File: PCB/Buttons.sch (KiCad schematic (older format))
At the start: 15 parts

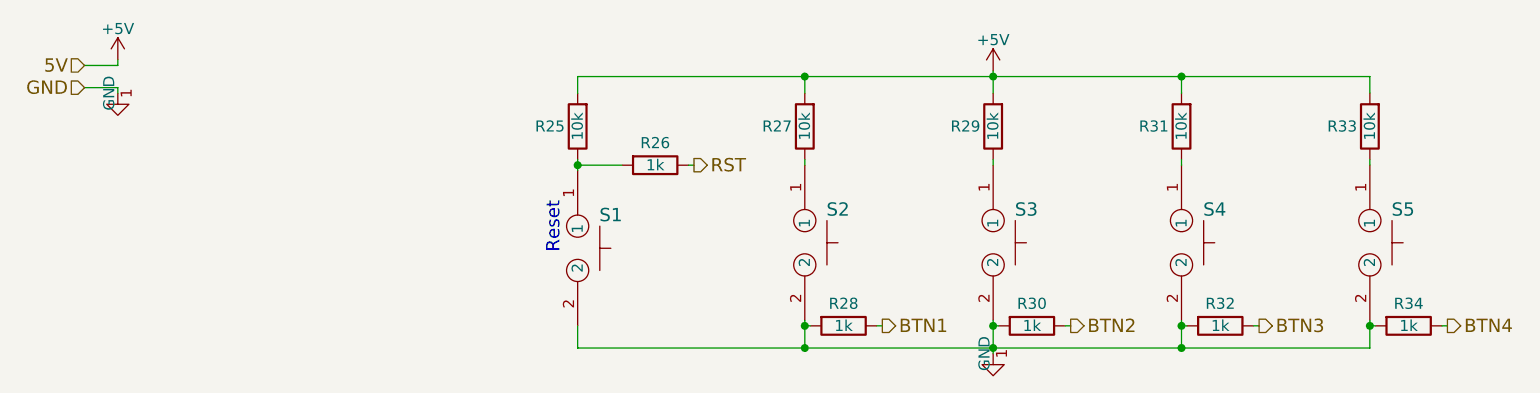
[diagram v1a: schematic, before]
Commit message: Added PCB layout
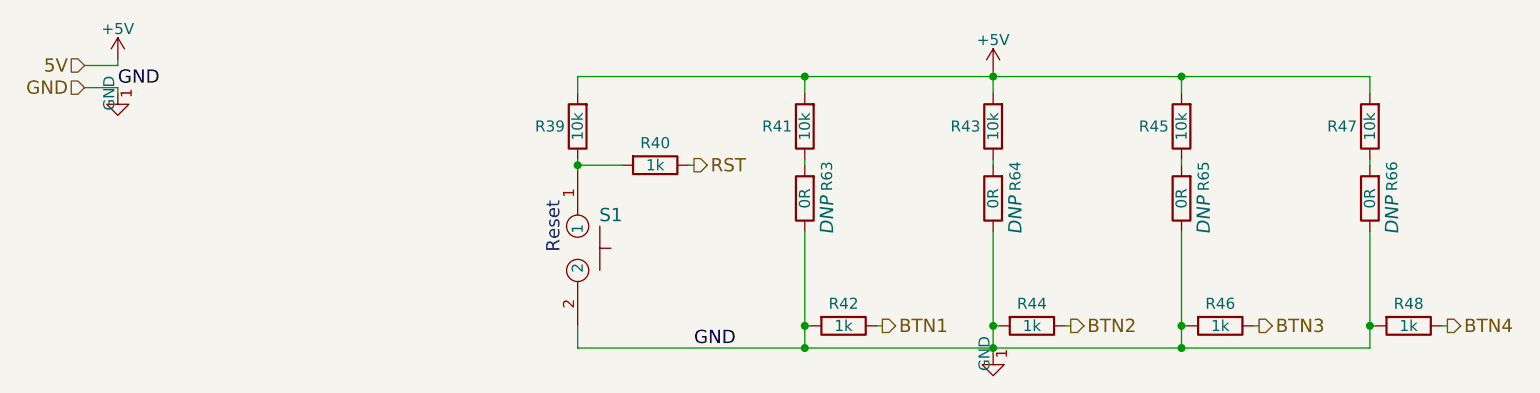
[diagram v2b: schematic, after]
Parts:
- removed S2, S3, S4, S5: mom_button, symbol mom_button
- added R63, R64, R65, R66: 0R, Resistor_THT:R_Axial_DIN0207_L6.3mm_D2.5mm_P2.54mm_Vertical, symbol R
- R39: renamed from R25; footprint (none) -> Resistors_SMD:R_0603_HandSoldering
- R40: renamed from R26; footprint (none) -> Resistors_SMD:R_0603_HandSoldering
- R41: renamed from R27; footprint (none) -> Resistors_SMD:R_0603_HandSoldering
- R42: renamed from R28; footprint (none) -> Resistors_SMD:R_0603_HandSoldering
- R43: renamed from R29; footprint (none) -> Resistors_SMD:R_0603_HandSoldering
- R44: renamed from R30; footprint (none) -> Resistors_SMD:R_0603_HandSoldering
- R45: renamed from R31; footprint (none) -> Resistors_SMD:R_0603_HandSoldering
- R46: renamed from R32; footprint (none) -> Resistors_SMD:R_0603_HandSoldering
- R47: renamed from R33; footprint (none) -> Resistors_SMD:R_0603_HandSoldering
- R48: renamed from R34; footprint (none) -> Resistors_SMD:R_0603_HandSoldering
- S1: footprint (none) -> Buttons_Switches_THT:SW_TH_Tactile_Omron_B3F-10xx
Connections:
- net GND: now also R42.2, R44.2, R46.2, R48.2, S1.2, R63.1, R64.1, R65.1, R66.1
- net at R41.1: now also R63.2
- net at R43.1: now also R64.2
- net at R45.1: now also R65.2
- net at R47.1: now also R66.2
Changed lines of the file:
@@
 $EndDescr
 $Comp
-L mom_button S1
-U 1 1 5A1EF454
-P 3450 3800
-F 0 "S1" V 3250 4000 60  0000 C CNN
-F 1 "mom_button" H 3450 3750 60  0001 C CNN
-F 2 "" H 3450 3800 60  0001 C CNN
-F 3 "" H 3450 3800 60  0001 C CNN
-	1    3450 3800
-	0    1    1    0
-$EndComp
-$Comp
-L R R25
+L R R39
 U 1 1 5A1EF45B
 P 3500 3200
-F 0 "R25" H 3625 3200 50  0000 C CNN
+F 0 "R39" H 3625 3200 50  0000 C CNN
 F 1 "10k" V 3500 3200 50  0000 C CNN
-F 2 "" V 3430 3200 50  0001 C CNN
+F 2 "Resistors_SMD:R_0603_HandSoldering" V 3430 3200 50  0001 C CNN
 F 3 "" H 3500 3200 50  0001 C CNN
 	1    3500 3200
@@
 $EndComp
 $Comp
-L R R26
+L R R40
 U 1 1 5A1EF462
 P 3850 3375
-F 0 "R26" V 3750 3375 50  0000 C CNN
+F 0 "R40" V 3750 3375 50  0000 C CNN
 F 1 "1k" V 3850 3375 50  0000 C CNN
-F 2 "" V 3780 3375 50  0001 C CNN
+F 2 "Resistors_SMD:R_0603_HandSoldering" V 3780 3375 50  0001 C CNN
 F 3 "" H 3850 3375 50  0001 C CNN
 	1    3850 3375
@@
 $EndComp
 $Comp
-L mom_button S2
-U 1 1 5A1EF476
-P 4475 3775
-F 0 "S2" V 4275 3975 60  0000 C CNN
-F 1 "mom_button" H 4475 3725 60  0001 C CNN
-F 2 "" H 4475 3775 60  0001 C CNN
-F 3 "" H 4475 3775 60  0001 C CNN
-	1    4475 3775
-	0    1    1    0
-$EndComp
-$Comp
-L R R27
+L R R41
 U 1 1 5A1EF47D
 P 4525 3200
-F 0 "R27" H 4650 3200 50  0000 C CNN
+F 0 "R41" H 4650 3200 50  0000 C CNN
 F 1 "10k" V 4525 3200 50  0000 C CNN
-F 2 "" V 4455 3200 50  0001 C CNN
+F 2 "Resistors_SMD:R_0603_HandSoldering" V 4455 3200 50  0001 C CNN
 F 3 "" H 4525 3200 50  0001 C CNN
 	1    4525 3200
@@
 $EndComp
 $Comp
-L R R28
+L R R42
 U 1 1 5A1EF484
 P 4700 4100
-F 0 "R28" V 4600 4100 50  0000 C CNN
+F 0 "R42" V 4600 4100 50  0000 C CNN
 F 1 "1k" V 4700 4100 50  0000 C CNN
-F 2 "" V 4630 4100 50  0001 C CNN
+F 2 "Resistors_SMD:R_0603_HandSoldering" V 4630 4100 50  0001 C CNN
 F 3 "" H 4700 4100 50  0001 C CNN
 	1    4700 4100
@@
 Reset
 $Comp
-L mom_button S3
-U 1 1 5A1EF499
-P 5325 3775
-F 0 "S3" V 5125 3975 60  0000 C CNN
-F 1 "mom_button" H 5325 3725 60  0001 C CNN
-F 2 "" H 5325 3775 60  0001 C CNN
-F 3 "" H 5325 3775 60  0001 C CNN
-	1    5325 3775
-	0    1    1    0
-$EndComp
-$Comp
-L R R29
+L R R43
 U 1 1 5A1EF4A0
 P 5375 3200
-F 0 "R29" H 5500 3200 50  0000 C CNN
+F 0 "R43" H 5500 3200 50  0000 C CNN
 F 1 "10k" V 5375 3200 50  0000 C CNN
-F 2 "" V 5305 3200 50  0001 C CNN
+F 2 "Resistors_SMD:R_0603_HandSoldering" V 5305 3200 50  0001 C CNN
 F 3 "" H 5375 3200 50  0001 C CNN
 	1    5375 3200
@@
 $EndComp
 $Comp
-L R R30
+L R R44
 U 1 1 5A1EF4A7
 P 5550 4100
-F 0 "R30" V 5450 4100 50  0000 C CNN
+F 0 "R44" V 5450 4100 50  0000 C CNN
 F 1 "1k" V 5550 4100 50  0000 C CNN
-F 2 "" V 5480 4100 50  0001 C CNN
+F 2 "Resistors_SMD:R_0603_HandSoldering" V 5480 4100 50  0001 C CNN
 F 3 "" H 5550 4100 50  0001 C CNN
 	1    5550 4100
@@
 $EndComp
 $Comp
-L mom_button S4
-U 1 1 5A1EF4BB
-P 6175 3775
-F 0 "S4" V 5975 3975 60  0000 C CNN
-F 1 "mom_button" H 6175 3725 60  0001 C CNN
-F 2 "" H 6175 3775 60  0001 C CNN
-F 3 "" H 6175 3775 60  0001 C CNN
-	1    6175 3775
-	0    1    1    0
-$EndComp
-$Comp
-L R R31
+L R R45
 U 1 1 5A1EF4C2
 P 6225 3200
-F 0 "R31" H 6350 3200 50  0000 C CNN
+F 0 "R45" H 6350 3200 50  0000 C CNN
 F 1 "10k" V 6225 3200 50  0000 C CNN
-F 2 "" V 6155 3200 50  0001 C CNN
+F 2 "Resistors_SMD:R_0603_HandSoldering" V 6155 3200 50  0001 C CNN
 F 3 "" H 6225 3200 50  0001 C CNN
 	1    6225 3200
@@
 $EndComp
 $Comp
-L R R32
+L R R46
 U 1 1 5A1EF4C9
 P 6400 4100
-F 0 "R32" V 6300 4100 50  0000 C CNN
+F 0 "R46" V 6300 4100 50  0000 C CNN
 F 1 "1k" V 6400 4100 50  0000 C CNN
-F 2 "" V 6330 4100 50  0001 C CNN
+F 2 "Resistors_SMD:R_0603_HandSoldering" V 6330 4100 50  0001 C CNN
 F 3 "" H 6400 4100 50  0001 C CNN
 	1    6400 4100
@@
 $EndComp
 $Comp
-L mom_button S5
-U 1 1 5A1EF4DD
-P 7025 3775
-F 0 "S5" V 6825 3975 60  0000 C CNN
-F 1 "mom_button" H 7025 3725 60  0001 C CNN
-F 2 "" H 7025 3775 60  0001 C CNN
-F 3 "" H 7025 3775 60  0001 C CNN
-	1    7025 3775
-	0    1    1    0
-$EndComp
-$Comp
-L R R33
+L R R47
 U 1 1 5A1EF4E4
 P 7075 3200
-F 0 "R33" H 7200 3200 50  0000 C CNN
+F 0 "R47" H 7200 3200 50  0000 C CNN
 F 1 "10k" V 7075 3200 50  0000 C CNN
-F 2 "" V 7005 3200 50  0001 C CNN
+F 2 "Resistors_SMD:R_0603_HandSoldering" V 7005 3200 50  0001 C CNN
 F 3 "" H 7075 3200 50  0001 C CNN
 	1    7075 3200
@@
 $EndComp
 $Comp
-L R R34
+L R R48
 U 1 1 5A1EF4EB
 P 7250 4100
-F 0 "R34" V 7150 4100 50  0000 C CNN
+F 0 "R48" V 7150 4100 50  0000 C CNN
 F 1 "1k" V 7250 4100 50  0000 C CNN
-F 2 "" V 7180 4100 50  0001 C CNN
+F 2 "Resistors_SMD:R_0603_HandSoldering" V 7180 4100 50  0001 C CNN
 F 3 "" H 7250 4100 50  0001 C CNN
 	1    7250 4100
@@
 GND
 $Comp
-L GND-RESCUE-Tardis #PWR063
+L GND-RESCUE-Tardis #PWR062
 U 1 1 5A341B2F
 P 1425 3050
-AR Path="/5A341B2F" Ref="#PWR063"  Part="1"
-AR Path="/5A1EEEAC/5A341B2F" Ref="#PWR67"  Part="1"
-F 0 "#PWR67" H 1425 2800 50  0001 C CNN
+F 0 "#PWR062" H 1425 2800 50  0001 C CNN
 F 1 "GND" H 1425 2900 50  0001 C CNN
 F 2 "" H 1425 3050 50  0001 C CNN
@@
 	1425 3025 1425 3050
 $Comp
-L +5V #PWR66
+L +5V #PWR063
 U 1 1 5A341B37
 P 1425 2900
-F 0 "#PWR66" H 1425 2750 50  0001 C CNN
+F 0 "#PWR063" H 1425 2750 50  0001 C CNN
 F 1 "+5V" H 1425 3040 50  0000 C CNN
 F 2 "" H 1425 2900 50  0001 C CNN
@@
 	3500 3350 3500 3400
 $Comp
-L +5V #PWR68
+L +5V #PWR064
 U 1 1 5A342622
 P 5375 2950
-F 0 "#PWR68" H 5375 2800 50  0001 C CNN
+F 0 "#PWR064" H 5375 2800 50  0001 C CNN
 F 1 "+5V" H 5375 3090 50  0000 C CNN
 F 2 "" H 5375 2950 50  0001 C CNN
@@
 $EndComp
 $Comp
-L GND-RESCUE-Tardis #PWR066
+L GND-RESCUE-Tardis #PWR065
 U 1 1 5A34265A
 P 5375 4225
-AR Path="/5A34265A" Ref="#PWR066"  Part="1"
-AR Path="/5A1EEEAC/5A34265A" Ref="#PWR69"  Part="1"
-F 0 "#PWR69" H 5375 3975 50  0001 C CNN
+F 0 "#PWR065" H 5375 3975 50  0001 C CNN
 F 1 "GND" H 5375 4075 50  0001 C CNN
 F 2 "" H 5375 4225 50  0001 C CNN
@@
 	4525 3350 4525 3375
 Wire Wire Line
-	4525 4075 4525 4200
+	4525 3675 4525 4200
 Wire Wire Line
 	4525 4100 4550 4100
@@
 	5400 4100 5375 4100
 Wire Wire Line
-	5375 4075 5375 4225
-Wire Wire Line
-	6225 4075 6225 4200
+	5375 3675 5375 4225
+Wire Wire Line
+	6225 4200 6225 3675
 Wire Wire Line
 	6225 4100 6250 4100
@@
 	7100 4100 7075 4100
 Wire Wire Line
-	7075 4200 7075 4075
+	7075 4200 7075 3675
 Wire Wire Line
 	7425 4100 7400 4100
@@
 	3700 3375 3500 3375
 Connection ~ 3500 3375
+Text Label 4025 4200 0    60   ~ 0
+GND
+Text Label 1425 3025 0    60   ~ 0
+GND
+$Comp
+L R R63
+U 1 1 5A4F3BCE
+P 4525 3525
+F 0 "R63" V 4425 3425 50  0000 C CNN
+F 1 "0R" V 4525 3525 50  0000 C CNN
+F 2 "Resistor_THT:R_Axial_DIN0207_L6.3mm_D2.5mm_P2.54mm_Vertical" V 4455 3525 50  0001 C CNN
+F 3 "" H 4525 3525 50  0001 C CNN
+F 4 "Jumper" V 4425 3600 39  0001 C CNN "%"
+F 5 "DNP" V 4425 3600 60  0000 C CIN "DNP"
+F 6 "A105988CT-ND" V 4525 3525 60  0001 C CNN "Digikey"
+	1    4525 3525
+	-1   0    0    1
+$EndComp
+$Comp
+L mom_button S1
+U 1 1 5A1EF454
+P 3450 3800
+F 0 "S1" V 3250 4000 60  0000 C CNN
+F 1 "mom_button" H 3450 3750 60  0001 C CNN
+F 2 "Buttons_Switches_THT:SW_TH_Tactile_Omron_B3F-10xx" H 3450 3800 60  0001 C CNN
+F 3 "" H 3450 3800 60  0001 C CNN
+	1    3450 3800
+	0    1    1    0
+$EndComp
+$Comp
+L R R64
+U 1 1 5A4F426C
+P 5375 3525
+F 0 "R64" V 5275 3425 50  0000 C CNN
+F 1 "0R" V 5375 3525 50  0000 C CNN
+F 2 "Resistor_THT:R_Axial_DIN0207_L6.3mm_D2.5mm_P2.54mm_Vertical" V 5305 3525 50  0001 C CNN
+F 3 "" H 5375 3525 50  0001 C CNN
+F 4 "Jumper" V 5275 3600 39  0001 C CNN "%"
+F 5 "DNP" V 5275 3600 60  0000 C CIN "DNP"
+F 6 "A105988CT-ND" V 5375 3525 60  0001 C CNN "Digikey"
+	1    5375 3525
+	-1   0    0    1
+$EndComp
+$Comp
+L R R65
+U 1 1 5A4F42ED
+P 6225 3525
+F 0 "R65" V 6125 3425 50  0000 C CNN
+F 1 "0R" V 6225 3525 50  0000 C CNN
+F 2 "Resistor_THT:R_Axial_DIN0207_L6.3mm_D2.5mm_P2.54mm_Vertical" V 6155 3525 50  0001 C CNN
+F 3 "" H 6225 3525 50  0001 C CNN
+F 4 "Jumper" V 6125 3600 39  0001 C CNN "%"
+F 5 "DNP" V 6125 3600 60  0000 C CIN "DNP"
+F 6 "A105988CT-ND" V 6225 3525 60  0001 C CNN "Digikey"
+	1    6225 3525
+	-1   0    0    1
+$EndComp
+$Comp
+L R R66
+U 1 1 5A4F4359
+P 7075 3525
+F 0 "R66" V 6975 3425 50  0000 C CNN
+F 1 "0R" V 7075 3525 50  0000 C CNN
+F 2 "Resistor_THT:R_Axial_DIN0207_L6.3mm_D2.5mm_P2.54mm_Vertical" V 7005 3525 50  0001 C CNN
+F 3 "" H 7075 3525 50  0001 C CNN
+F 4 "Jumper" V 6975 3600 39  0001 C CNN "%"
+F 5 "DNP" V 6975 3600 60  0000 C CIN "DNP"
+F 6 "A105988CT-ND" V 7075 3525 60  0001 C CNN "Digikey"
+	1    7075 3525
+	-1   0    0    1
+$EndComp
 $EndSCHEMATC

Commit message: ./
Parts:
- removed R63, R64, R65, R66: 0R, Resistor_THT:R_Axial_DIN0207_L6.3mm_D2.5mm_P2.54mm_Vertical, symbol R
- added R10, R11, R12, R13: 0R, Resistor_THT:R_Axial_DIN0204_L3.6mm_D1.6mm_P2.54mm_Vertical, symbol R
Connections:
- net GND: no longer R42.2, R44.2, R46.2, R48.2
- net at R41.1: now also R10.2
- net at R43.1: now also R11.2
- net at R45.1: now also R12.2
- net at R47.1: now also R13.2
- new net: R10.1, R42.2
- new net: R11.1, R44.2
- new net: R12.1, R46.2
- new net: R13.1, R48.2
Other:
- moved on the sheet: R42, R44, R46, R48
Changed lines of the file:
@@
 L R R42
 U 1 1 5A1EF484
-P 4700 4100
-F 0 "R42" V 4600 4100 50  0000 C CNN
-F 1 "1k" V 4700 4100 50  0000 C CNN
-F 2 "Resistors_SMD:R_0603_HandSoldering" V 4630 4100 50  0001 C CNN
-F 3 "" H 4700 4100 50  0001 C CNN
-	1    4700 4100
+P 4675 3800
+F 0 "R42" V 4575 3800 50  0000 C CNN
+F 1 "1k" V 4675 3800 50  0000 C CNN
+F 2 "Resistors_SMD:R_0603_HandSoldering" V 4605 3800 50  0001 C CNN
+F 3 "" H 4675 3800 50  0001 C CNN
+	1    4675 3800
 	0    1    1    0
 $EndComp
@@
 L R R44
 U 1 1 5A1EF4A7
-P 5550 4100
-F 0 "R44" V 5450 4100 50  0000 C CNN
-F 1 "1k" V 5550 4100 50  0000 C CNN
-F 2 "Resistors_SMD:R_0603_HandSoldering" V 5480 4100 50  0001 C CNN
-F 3 "" H 5550 4100 50  0001 C CNN
-	1    5550 4100
+P 5525 3800
+F 0 "R44" V 5425 3800 50  0000 C CNN
+F 1 "1k" V 5525 3800 50  0000 C CNN
+F 2 "Resistors_SMD:R_0603_HandSoldering" V 5455 3800 50  0001 C CNN
+F 3 "" H 5525 3800 50  0001 C CNN
+	1    5525 3800
 	0    1    1    0
 $EndComp
@@
 L R R46
 U 1 1 5A1EF4C9
-P 6400 4100
-F 0 "R46" V 6300 4100 50  0000 C CNN
-F 1 "1k" V 6400 4100 50  0000 C CNN
-F 2 "Resistors_SMD:R_0603_HandSoldering" V 6330 4100 50  0001 C CNN
-F 3 "" H 6400 4100 50  0001 C CNN
-	1    6400 4100
+P 6375 3800
+F 0 "R46" V 6275 3800 50  0000 C CNN
+F 1 "1k" V 6375 3800 50  0000 C CNN
+F 2 "Resistors_SMD:R_0603_HandSoldering" V 6305 3800 50  0001 C CNN
+F 3 "" H 6375 3800 50  0001 C CNN
+	1    6375 3800
 	0    1    1    0
 $EndComp
@@
 L R R48
 U 1 1 5A1EF4EB
-P 7250 4100
-F 0 "R48" V 7150 4100 50  0000 C CNN
-F 1 "1k" V 7250 4100 50  0000 C CNN
-F 2 "Resistors_SMD:R_0603_HandSoldering" V 7180 4100 50  0001 C CNN
-F 3 "" H 7250 4100 50  0001 C CNN
-	1    7250 4100
+P 7225 3800
+F 0 "R48" V 7125 3800 50  0000 C CNN
+F 1 "1k" V 7225 3800 50  0000 C CNN
+F 2 "Resistors_SMD:R_0603_HandSoldering" V 7155 3800 50  0001 C CNN
+F 3 "" H 7225 3800 50  0001 C CNN
+	1    7225 3800
 	0    1    1    0
 $EndComp
 Text HLabel 4025 3375 2    60   Output ~ 0
 RST
-Text HLabel 4875 4100 2    60   Output ~ 0
+Text HLabel 4850 3800 2    60   Output ~ 0
 BTN1
-Text HLabel 5725 4100 2    60   Output ~ 0
+Text HLabel 5700 3800 2    60   Output ~ 0
 BTN2
-Text HLabel 6575 4100 2    60   Output ~ 0
+Text HLabel 6550 3800 2    60   Output ~ 0
 BTN3
-Text HLabel 7425 4100 2    60   Output ~ 0
+Text HLabel 7400 3800 2    60   Output ~ 0
 BTN4
 Text HLabel 1275 3025 0    60   Input ~ 0
 GND
 $Comp
-L GND-RESCUE-Tardis #PWR062
+L GND-RESCUE-Tardis #PWR63
 U 1 1 5A341B2F
 P 1425 3050
-F 0 "#PWR062" H 1425 2800 50  0001 C CNN
+F 0 "#PWR63" H 1425 2800 50  0001 C CNN
 F 1 "GND" H 1425 2900 50  0001 C CNN
 F 2 "" H 1425 3050 50  0001 C CNN
@@
 	1425 3025 1425 3050
 $Comp
-L +5V #PWR063
+L +5V #PWR62
 U 1 1 5A341B37
 P 1425 2900
-F 0 "#PWR063" H 1425 2750 50  0001 C CNN
+F 0 "#PWR62" H 1425 2750 50  0001 C CNN
 F 1 "+5V" H 1425 3040 50  0000 C CNN
 F 2 "" H 1425 2900 50  0001 C CNN
@@
 	3500 3350 3500 3400
 $Comp
-L +5V #PWR064
+L +5V #PWR65
 U 1 1 5A342622
 P 5375 2950
-F 0 "#PWR064" H 5375 2800 50  0001 C CNN
+F 0 "#PWR65" H 5375 2800 50  0001 C CNN
 F 1 "+5V" H 5375 3090 50  0000 C CNN
 F 2 "" H 5375 2950 50  0001 C CNN
@@
 $EndComp
 $Comp
-L GND-RESCUE-Tardis #PWR065
+L GND-RESCUE-Tardis #PWR64
 U 1 1 5A34265A
-P 5375 4225
-F 0 "#PWR065" H 5375 3975 50  0001 C CNN
-F 1 "GND" H 5375 4075 50  0001 C CNN
-F 2 "" H 5375 4225 50  0001 C CNN
-F 3 "" H 5375 4225 50  0001 C CNN
-	1    5375 4225
-	1    0    0    -1
-$EndComp
-Wire Wire Line
-	4525 3350 4525 3375
-Wire Wire Line
-	4525 3675 4525 4200
-Wire Wire Line
-	4525 4100 4550 4100
-Wire Wire Line
-	4850 4100 4875 4100
-Wire Wire Line
-	5700 4100 5725 4100
-Wire Wire Line
-	5400 4100 5375 4100
-Wire Wire Line
-	5375 3675 5375 4225
-Wire Wire Line
-	6225 4200 6225 3675
-Wire Wire Line
-	6225 4100 6250 4100
-Wire Wire Line
-	6550 4100 6575 4100
-Wire Wire Line
-	6225 3375 6225 3350
-Wire Wire Line
-	7100 4100 7075 4100
-Wire Wire Line
-	7075 4200 7075 3675
-Wire Wire Line
-	7425 4100 7400 4100
-Wire Wire Line
-	7075 3375 7075 3350
+P 3500 4200
+F 0 "#PWR64" H 3500 3950 50  0001 C CNN
+F 1 "GND" H 3500 4050 50  0001 C CNN
+F 2 "" H 3500 4200 50  0001 C CNN
+F 3 "" H 3500 4200 50  0001 C CNN
+	1    3500 4200
+	1    0    0    -1
+$EndComp
+Wire Wire Line
+	4825 3800 4850 3800
+Wire Wire Line
+	5675 3800 5700 3800
+Wire Wire Line
+	6525 3800 6550 3800
+Wire Wire Line
+	7400 3800 7375 3800
 Wire Wire Line
 	3500 3050 3500 2975
@@
 Connection ~ 4525 2975
 Wire Wire Line
-	3500 4200 7075 4200
-Connection ~ 7075 4100
-Connection ~ 5375 4200
-Connection ~ 5375 4100
-Connection ~ 4525 4200
-Connection ~ 4525 4100
-Connection ~ 6225 4200
-Connection ~ 6225 4100
-Wire Wire Line
-	5375 3350 5375 3375
-Wire Wire Line
 	3700 3375 3500 3375
 Connection ~ 3500 3375
-Text Label 4025 4200 0    60   ~ 0
+Text Label 3500 4150 0    60   ~ 0
 GND
 Text Label 1425 3025 0    60   ~ 0
 GND
-$Comp
-L R R63
-U 1 1 5A4F3BCE
-P 4525 3525
-F 0 "R63" V 4425 3425 50  0000 C CNN
-F 1 "0R" V 4525 3525 50  0000 C CNN
-F 2 "Resistor_THT:R_Axial_DIN0207_L6.3mm_D2.5mm_P2.54mm_Vertical" V 4455 3525 50  0001 C CNN
-F 3 "" H 4525 3525 50  0001 C CNN
-F 4 "Jumper" V 4425 3600 39  0001 C CNN "%"
-F 5 "DNP" V 4425 3600 60  0000 C CIN "DNP"
-F 6 "A105988CT-ND" V 4525 3525 60  0001 C CNN "Digikey"
-	1    4525 3525
-	-1   0    0    1
-$EndComp
 $Comp
 L mom_button S1
@@
 $EndComp
 $Comp
-L R R64
-U 1 1 5A4F426C
+L R R10
+U 1 1 5A59E758
+P 4525 3525
+F 0 "R10" H 4425 3525 50  0000 C CNN
+F 1 "0R" V 4525 3525 50  0000 C CNN
+F 2 "Resistor_THT:R_Axial_DIN0204_L3.6mm_D1.6mm_P2.54mm_Vertical" V 4455 3525 50  0001 C CNN
+F 3 "" H 4525 3525 50  0001 C CNN
+	1    4525 3525
+	-1   0    0    1
+$EndComp
+Wire Wire Line
+	4525 3350 4525 3375
+Wire Wire Line
+	4525 3675 4525 3800
+Wire Wire Line
+	5375 3350 5375 3375
+Wire Wire Line
+	5375 3675 5375 3800
+Wire Wire Line
+	6225 3350 6225 3375
+Wire Wire Line
+	6225 3675 6225 3800
+Wire Wire Line
+	7075 3675 7075 3800
+Wire Wire Line
+	7075 3375 7075 3350
+$Comp
+L R R11
+U 1 1 5A5A04BC
 P 5375 3525
-F 0 "R64" V 5275 3425 50  0000 C CNN
+F 0 "R11" H 5275 3525 50  0000 C CNN
 F 1 "0R" V 5375 3525 50  0000 C CNN
-F 2 "Resistor_THT:R_Axial_DIN0207_L6.3mm_D2.5mm_P2.54mm_Vertical" V 5305 3525 50  0001 C CNN
+F 2 "Resistor_THT:R_Axial_DIN0204_L3.6mm_D1.6mm_P2.54mm_Vertical" V 5305 3525 50  0001 C CNN
 F 3 "" H 5375 3525 50  0001 C CNN
-F 4 "Jumper" V 5275 3600 39  0001 C CNN "%"
-F 5 "DNP" V 5275 3600 60  0000 C CIN "DNP"
-F 6 "A105988CT-ND" V 5375 3525 60  0001 C CNN "Digikey"
 	1    5375 3525
 	-1   0    0    1
 $EndComp
 $Comp
-L R R65
-U 1 1 5A4F42ED
+L R R12
+U 1 1 5A5A0523
 P 6225 3525
-F 0 "R65" V 6125 3425 50  0000 C CNN
+F 0 "R12" H 6125 3525 50  0000 C CNN
 F 1 "0R" V 6225 3525 50  0000 C CNN
-F 2 "Resistor_THT:R_Axial_DIN0207_L6.3mm_D2.5mm_P2.54mm_Vertical" V 6155 3525 50  0001 C CNN
+F 2 "Resistor_THT:R_Axial_DIN0204_L3.6mm_D1.6mm_P2.54mm_Vertical" V 6155 3525 50  0001 C CNN
 F 3 "" H 6225 3525 50  0001 C CNN
-F 4 "Jumper" V 6125 3600 39  0001 C CNN "%"
-F 5 "DNP" V 6125 3600 60  0000 C CIN "DNP"
-F 6 "A105988CT-ND" V 6225 3525 60  0001 C CNN "Digikey"
 	1    6225 3525
 	-1   0    0    1
 $EndComp
 $Comp
-L R R66
-U 1 1 5A4F4359
+L R R13
+U 1 1 5A5A057B
 P 7075 3525
-F 0 "R66" V 6975 3425 50  0000 C CNN
+F 0 "R13" H 6975 3525 50  0000 C CNN
 F 1 "0R" V 7075 3525 50  0000 C CNN
-F 2 "Resistor_THT:R_Axial_DIN0207_L6.3mm_D2.5mm_P2.54mm_Vertical" V 7005 3525 50  0001 C CNN
+F 2 "Resistor_THT:R_Axial_DIN0204_L3.6mm_D1.6mm_P2.54mm_Vertical" V 7005 3525 50  0001 C CNN
 F 3 "" H 7075 3525 50  0001 C CNN
-F 4 "Jumper" V 6975 3600 39  0001 C CNN "%"
-F 5 "DNP" V 6975 3600 60  0000 C CIN "DNP"
-F 6 "A105988CT-ND" V 7075 3525 60  0001 C CNN "Digikey"
 	1    7075 3525
 	-1   0    0    1
